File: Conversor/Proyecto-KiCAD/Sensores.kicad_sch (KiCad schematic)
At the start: 6 parts

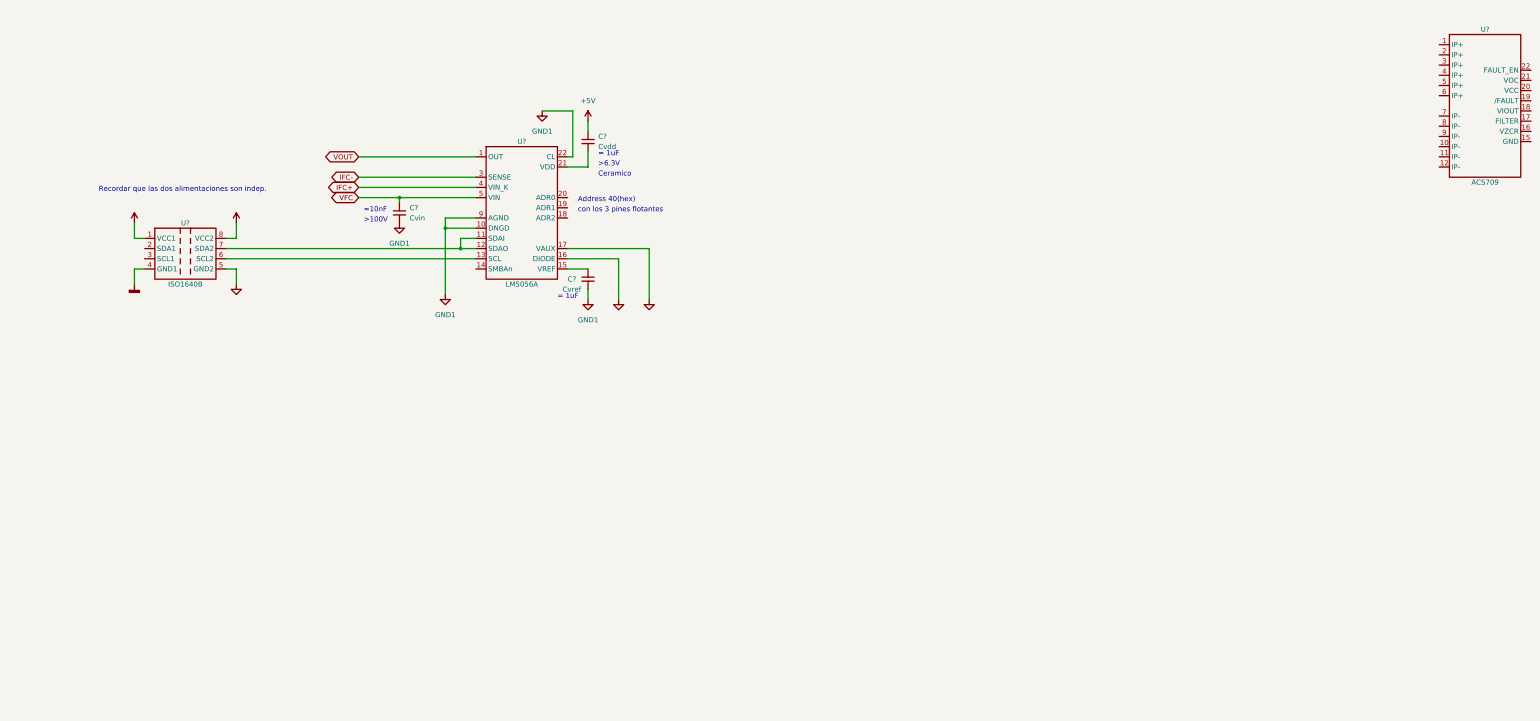
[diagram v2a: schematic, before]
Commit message: Seguir con el esquematico de los sensores
- Terminadas las conexiones del LM5056A para Iin/Vin/Vout
- Para el sensor de efecto hall ACS709, falta el acondicionamiento:
  - La tension de salida para 0A (Quiescent output voltage) es Vcc/2=2.5V.
  - Para X20BB, 4.5A (Imax+10%) se traducen a 252mV y 344 valores del ADC
    (osea de 2.5V a 2.752V).
  - Para X6BB, 4.5A se traducen a 474mV y 647 valores del ADC.
    (osea de 2.5V a 2.974V)
  - Preguntar si conviene restarle 2.5V y luego amplificar la señal a los
    3V del ADC para aumentar la resolucion, o quedarse con los 250/500 mV.
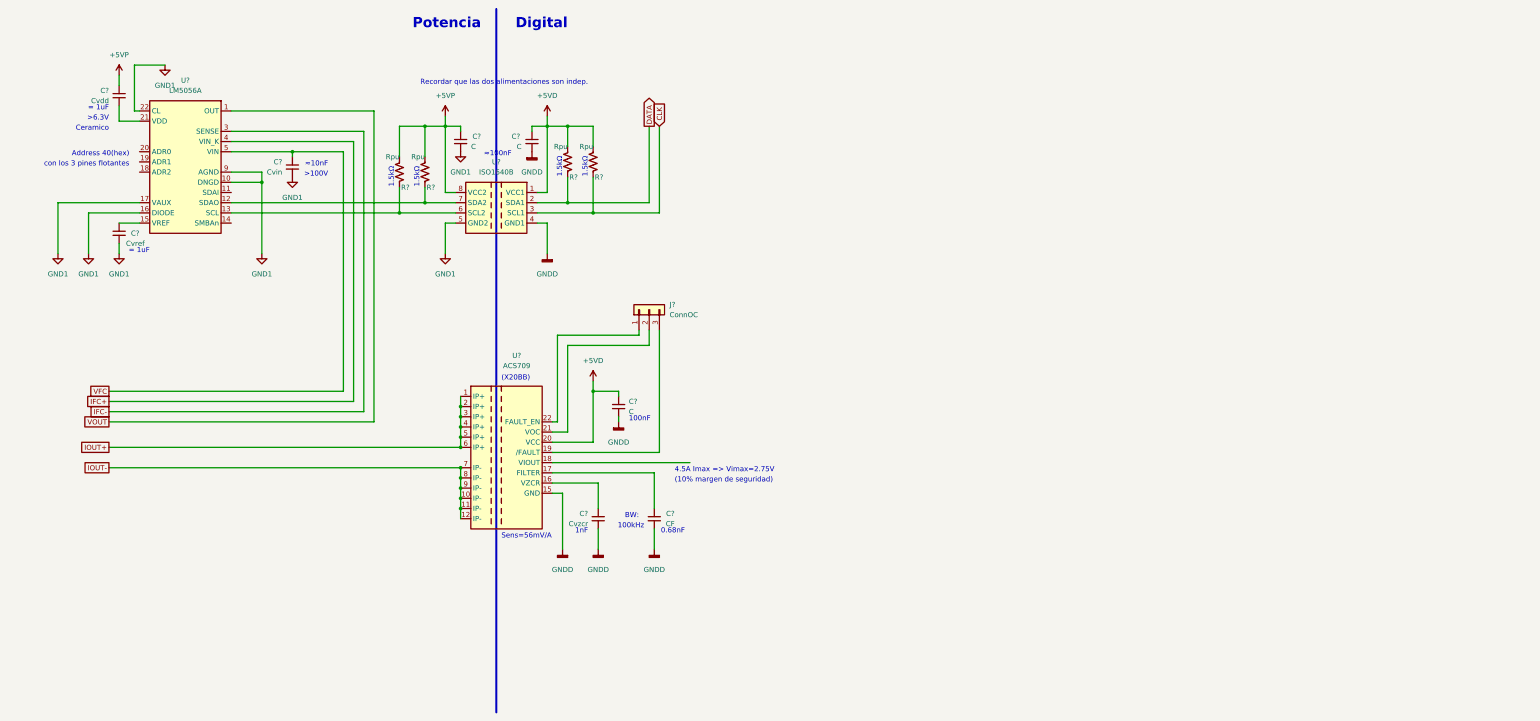
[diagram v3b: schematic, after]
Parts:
- removed U?: LM5056A, symbol Componentes proyecto:LM5056A
- removed U?: ACS709, symbol Componentes proyecto:ACS709
- removed U?: ISO1640B, symbol Componentes proyecto:ISO1640B
- added C?: CF, symbol Device:C_Small
- added C? (x3): C, symbol Device:C_Small
- added C?: Cvzcr, symbol Device:C_Small
- added J?: ConnOC, symbol Connector_Generic:Conn_01x03
- added R? (x4): Rpu, symbol Device:R_US
- added U?: ACS709, symbol Componentes proyecto:ACS709
- added U?: LM5056A, symbol Componentes proyecto:LM5056A
- added U?: ISO1640B, symbol Componentes proyecto:ISO1640B
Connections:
- net GND1: now also C?.2, U?.10 (DNGD), U?.16 (DIODE), U?.17 (VAUX), U?.22 (CL), U?.5 (GND2), U?.9 (AGND)
- net GNDD: now also C?.2, C?.2, C?.2, C?.2, U?.15 (GND), U?.4 (GND1)
- net IFC+: now also U?.4 (VIN_K)
- net IFC-: now also U?.3 (SENSE)
- net VFC: now also U?.5 (VIN)
- net VOUT: now also U?.1 (OUT)
- net at C?.1: now also U?.15 (VREF)
- net at C?.2: now also U?.21 (VDD)
- net +5V renamed +5VP
- net +5VP: now also C?.1, R?.1, R?.1, U?.8 (VCC2)
- new net: R?.2, U?.13 (SCL), U?.6 (SCL2)
- new net: R?.2, U?.12 (SDAO), U?.7 (SDA2)
- new net: C?.1, U?.17 (FILTER)
- new net: C?.1, U?.16 (VZCR)
- new net: J?.3 (Pin_3), U?.19 (/FAULT)
- new net: J?.2 (Pin_2), U?.21 (VOC)
- new net: J?.1 (Pin_1), U?.22 (FAULT_EN)
- new net +5VD: C?.1, C?.1, R?.1, R?.1, U?.1 (VCC1), U?.20 (VCC)
- new net CLK: R?.2, U?.3 (SCL1)
- new net DATA: R?.2, U?.2 (SDA1)
- new net IOUT+: U?.1 (IP+), U?.2 (IP+), U?.3 (IP+), U?.4 (IP+), U?.5 (IP+), U?.6 (IP+)
- new net IOUT-: U?.10 (IP-), U?.11 (IP-), U?.12 (IP-), U?.7 (IP-), U?.8 (IP-), U?.9 (IP-)
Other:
- note added: "(10% margen de seguridad)"
- note added: "(X20BB)"
- note added: "0.68nF"
- note added: "1.5kΩ"
- note added: "100kHz"
- note added: "100nF"
- note added: "1nF"
- note added: "4.5A Imax => Vimax=2.75V"
- note added: "BW:"
- note added: "Digital"
- note added: "Potencia"
- note added: "Sens=56mV/A"
- note added: "≈100nF"
- moved on the sheet: C?

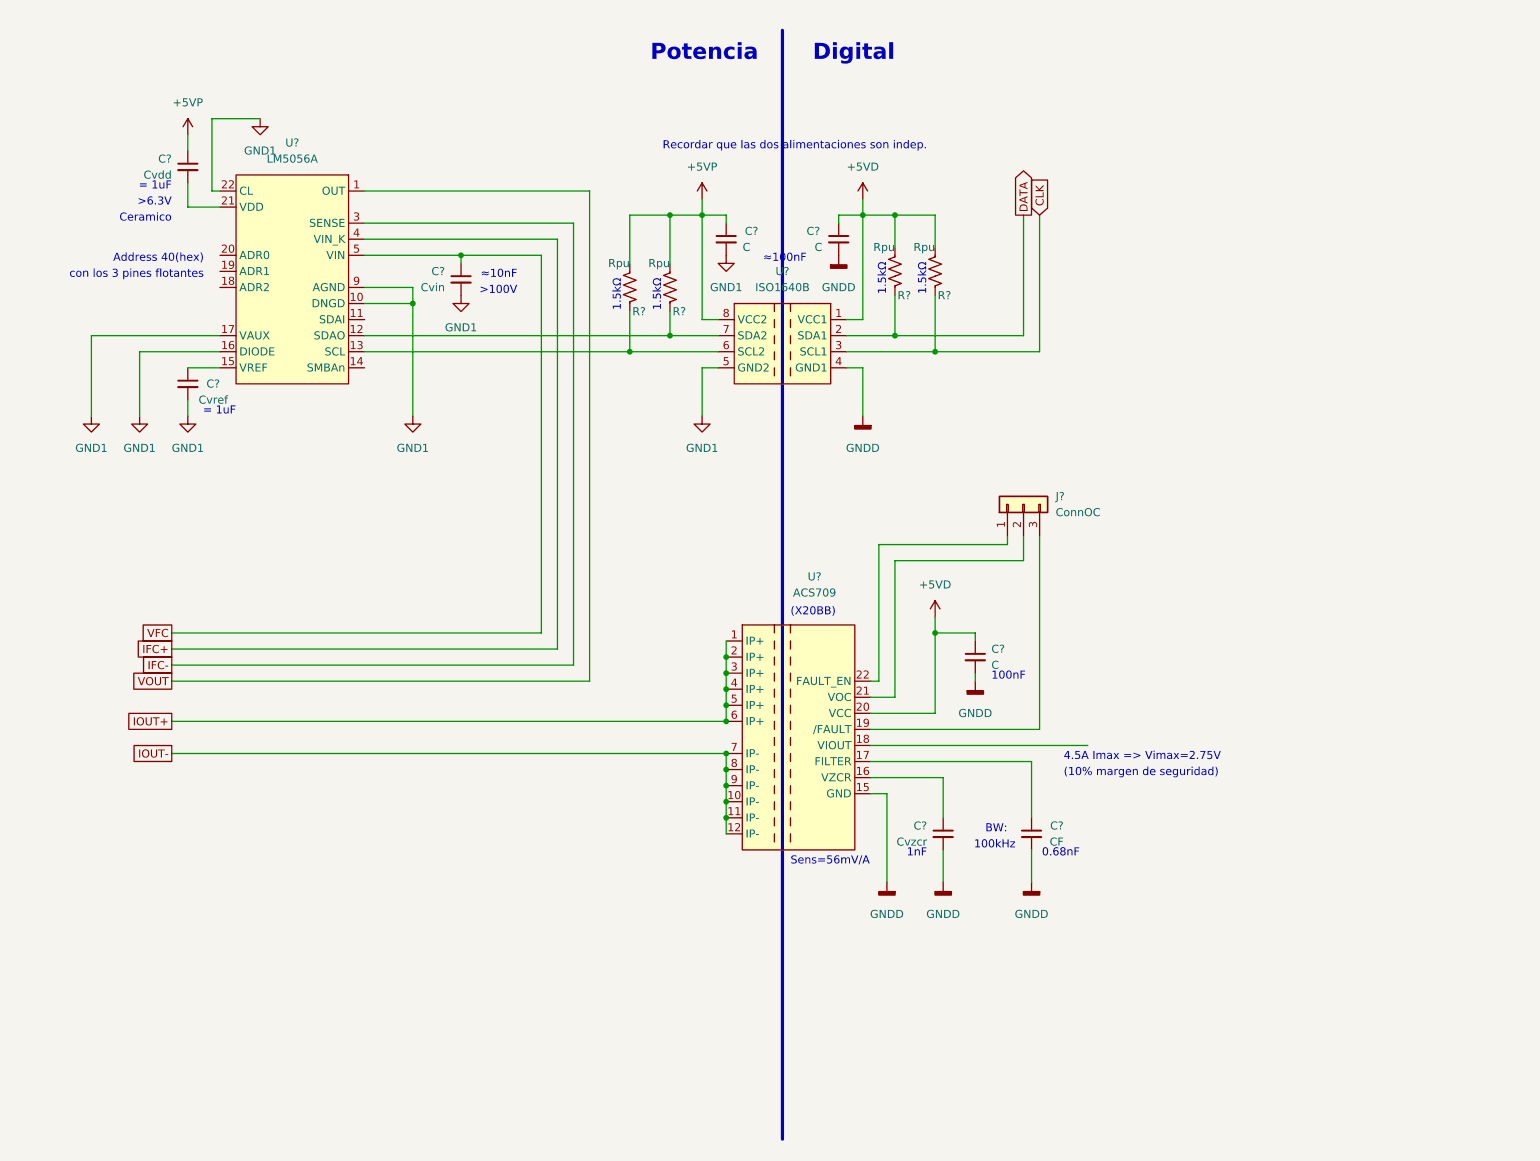
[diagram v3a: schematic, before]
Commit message: Casi terminada la parte de sensores (faltan valores)
- Faltan valores del circuito de acondicionamiento del ACS709 (difference amp.).
- Ver si se usa el mismo TLC2272 que en el diseño de referencia (agregada su datasheet).
- Agregada la bibliografia usada para entender el circuito de acondicionamiento.
- Agregadas las footprints de los integrados.
- Creada la sheet para las fuentes de alimentación.
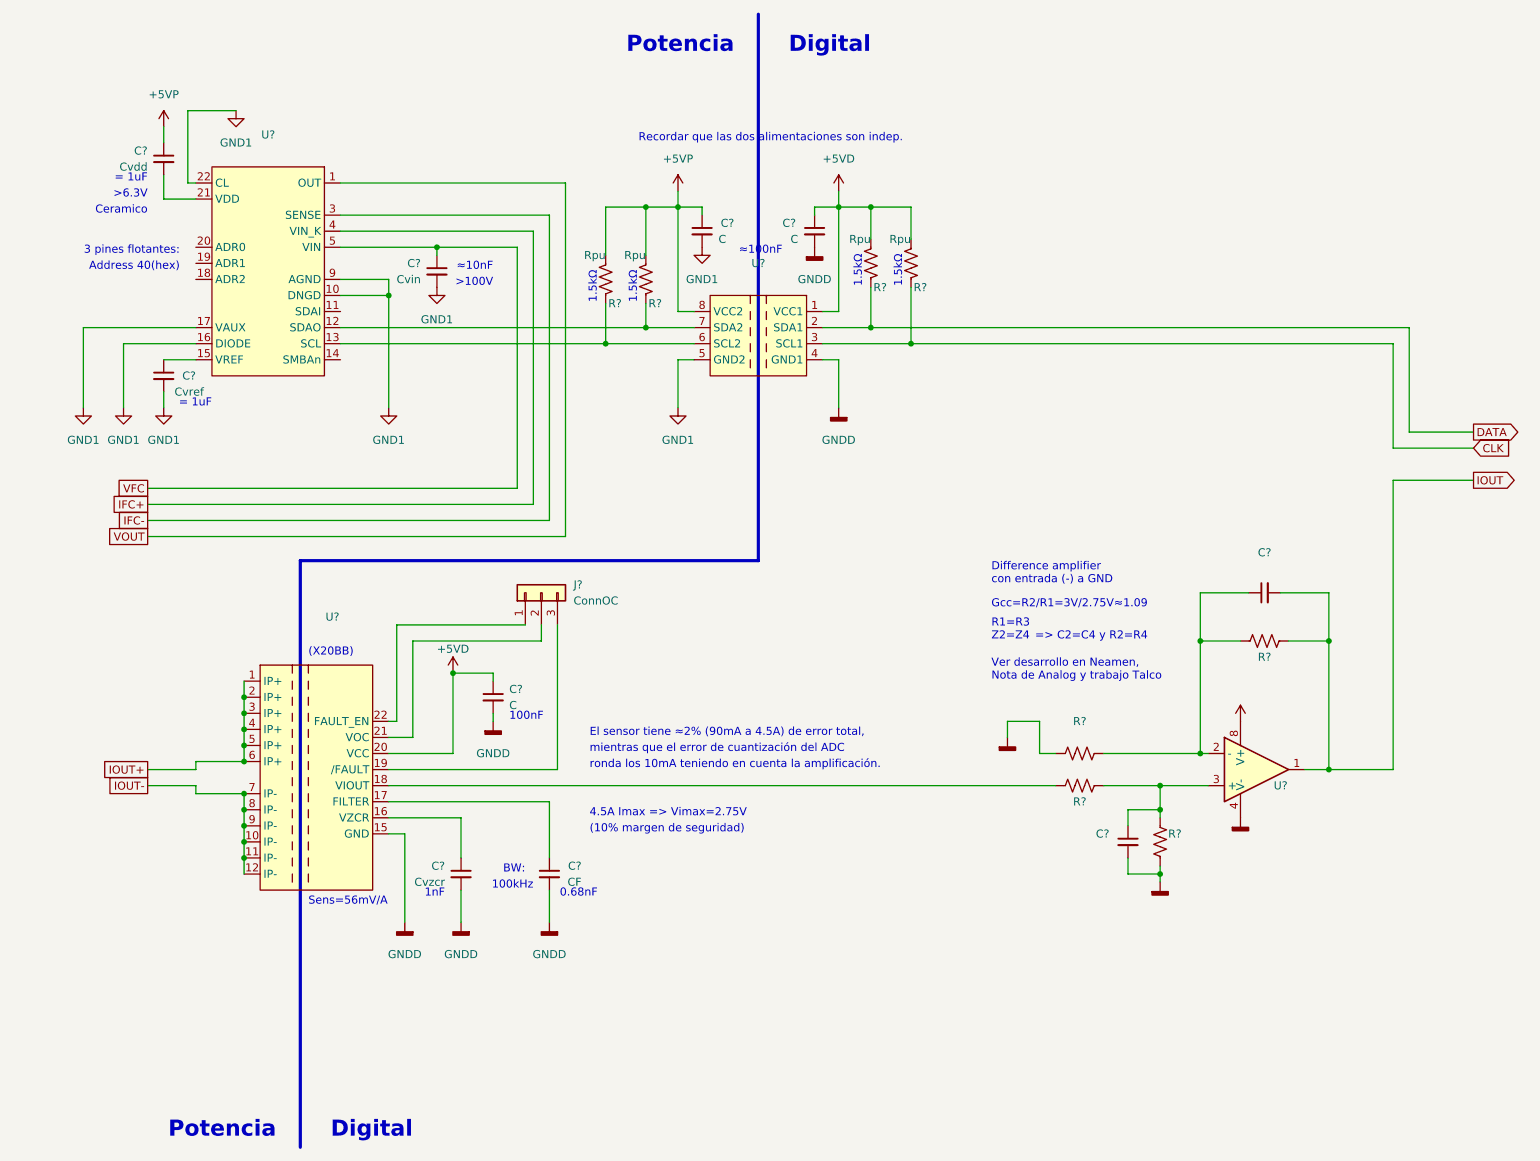
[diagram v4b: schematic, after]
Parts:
- added C? (x2): (no value), symbol Device:C_Small
- added R? (x4): (no value), symbol Device:R_US
- added U?: (no value), symbol Componentes proyecto:TLC2272
- U?: value ACS709 -> (none)
- U?: value LM5056A -> (none)
- U?: value ISO1640B -> (none)
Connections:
- net +5VD: now also U?.8 (V+)
- net GNDD: now also C?.2, R?.1, R?.2, U?.4 (V-)
- net at U?.18 (VIOUT): now also R?.1
- new net: C?.1, R?.1, R?.2, U?.2 (-)
- new net: C?.1, R?.1, R?.2, U?.3 (+)
- new net IOUT: C?.2, R?.2, U?.1
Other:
- note added: "3 pines flotantes:"
- note added: "=> C2=C4 y R2=R4"
- note added: "Difference amplifier con entrada (-) a GND"
- note added: "El sensor tiene ≈2% (90mA a 4.5A) de error total,"
- note added: "Gcc=R2/R1=3V/2.75V≈1.09"
- note added: "R1=R3 Z2=Z4"
- note added: "Ver desarrollo en Neamen, Nota de Analog y trabajo Talco"
- note added: "mientras que el error de cuantización del ADC"
- note added: "ronda los 10mA teniendo en cuenta la amplificación."
- note removed: "con los 3 pines flotantes"
- moved on the sheet: C?, J?, R?, U?
